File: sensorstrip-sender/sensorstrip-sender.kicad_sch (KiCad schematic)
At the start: 10 parts, among them J1 USB_C_Receptacle_PowerOnly, J2 Conn_01x02_MountingPin, SW1 SW_DPDT_x2

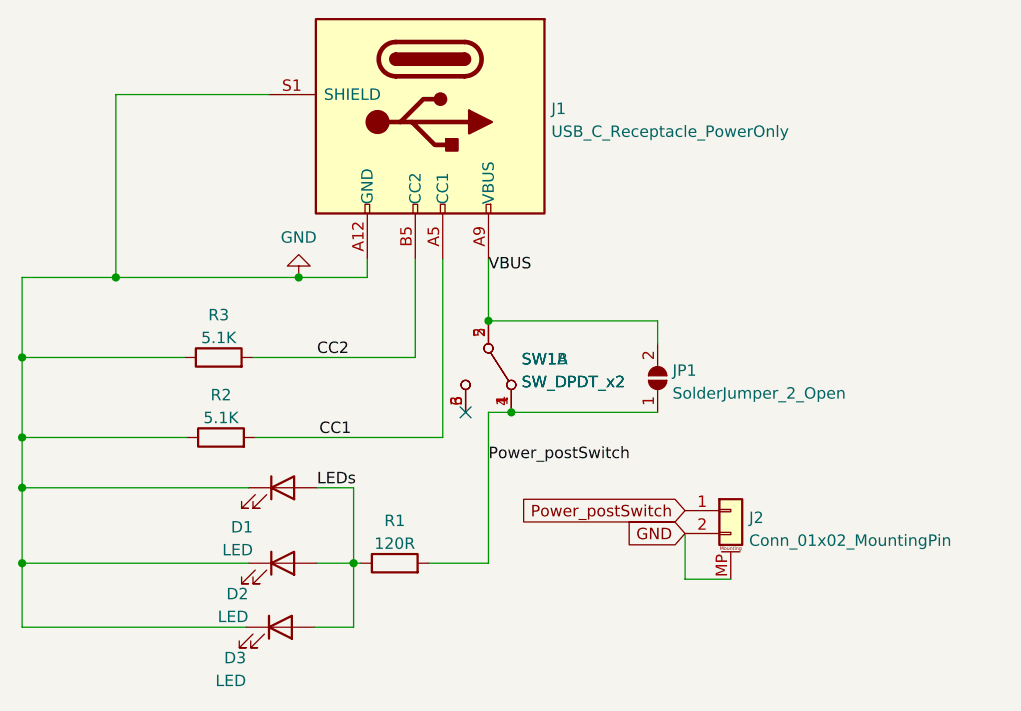
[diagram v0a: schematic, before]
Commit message: v3 (for real this time):
- Differentiate 'sender' and 'receiver' boards and allow daisy chaining receivers
- Update LED footprint to allow for more mounting options
- Swap to Molex Picoblade 53261 connector for ease of assembly
- Add PTH mounting holes to allow stacking boards for larger LEDs, or mounting with screws
- Add PPTC for overcurrent protection
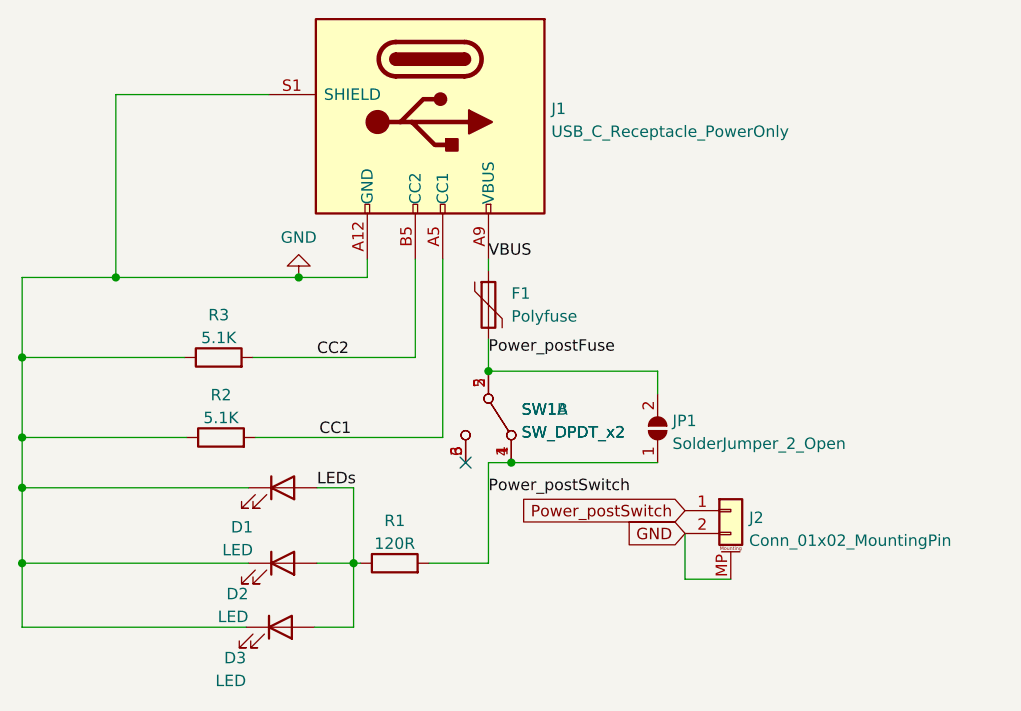
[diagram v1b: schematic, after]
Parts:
- added F1: Polyfuse, Fuse:Fuse_0805_2012Metric_Pad1.15x1.40mm_HandSolder, symbol Device:Polyfuse
- D1, D2, D3: footprint sensorstrip:LED_THT-1.27mm-OrthogonalSMDMount -> sensorstrip:LED_THT-1.27mm-OrthogonalSMDAndTHT
- J2: footprint Connector_JST:JST_GH_SM02B-GHS-TB_1x02-1MP_P1.25mm_Horizontal -> Connector_Molex:Molex_PicoBlade_53261-0271_1x02-1MP_P1.25mm_Horizontal
- R1: footprint Resistor_SMD:R_0603_1608Metric_Pad0.98x0.95mm_HandSolder -> Resistor_SMD:R_0805_2012Metric_Pad1.20x1.40mm_HandSolder
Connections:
- net VBUS: now also F1.1; no longer JP1.2 (B), SW1.2 (B), SW1.5 (B)
- new net Power_postFuse: F1.2, JP1.2 (B), SW1.2 (B), SW1.5 (B)
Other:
- moved on the sheet: JP1, SW1A, SW1B
